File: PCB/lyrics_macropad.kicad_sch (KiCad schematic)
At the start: 8 parts, among them SW1 SW_Push, SW2 SW_Push, SW3 SW_Push, SW4 SW_Push, SW5 SW_Push, U1 XIAO-RP2040-DIP

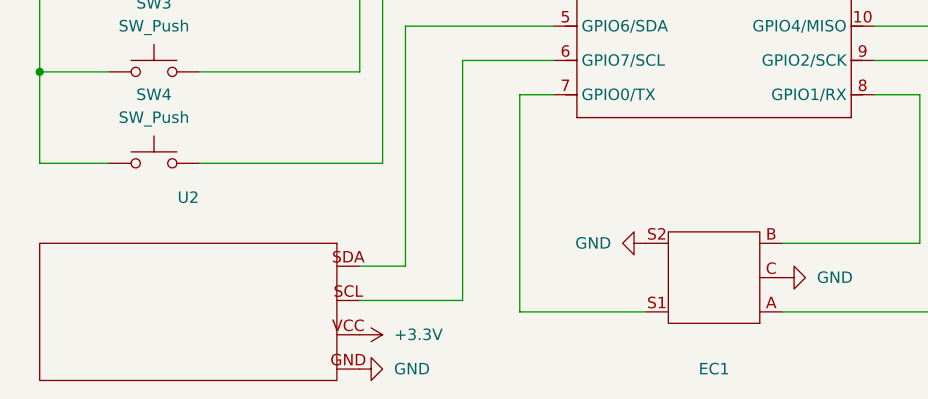
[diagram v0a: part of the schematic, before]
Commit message: Add CAD files and update PCB
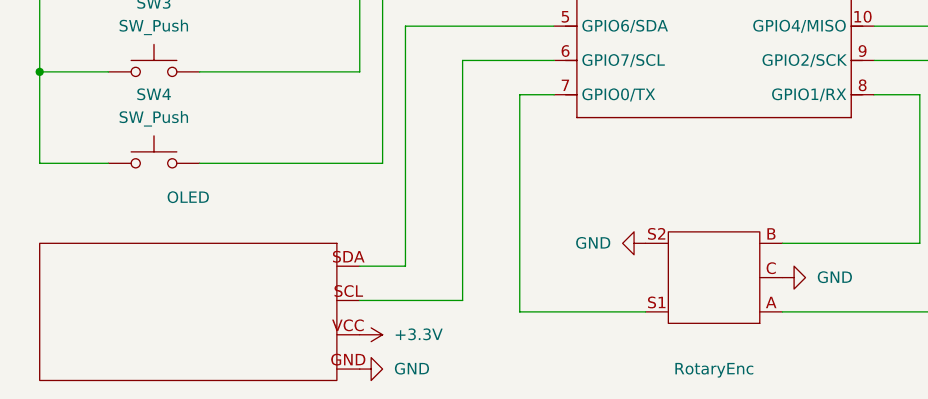
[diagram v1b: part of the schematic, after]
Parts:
- renumbered U2 to OLED, EC1 to RotaryEnc
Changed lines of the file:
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@@
 		(dnp no)
 		(fields_autoplaced yes)
-		(property "Reference" "U2"
+		(property "Reference" "OLED"
 			(at 93.98 90.17 0)
 			(effects
@@
 			(project ""
 				(path "/fcce1192-ab6a-46a7-9fac-1646581195fc"
-					(reference "U2")
+					(reference "OLED")
 					(unit 1)
 				)
@@
 		(on_board yes)
 		(dnp no)
-		(property "Reference" "EC1"
+		(property "Reference" "RotaryEnc"
 			(at 152.4 109.22 0)
 			(effects
@@
 			(project ""
 				(path "/fcce1192-ab6a-46a7-9fac-1646581195fc"
-					(reference "EC1")
-					(unit 1)
-				)
+					(reference "RotaryEnc")
+					(unit 1)
+				)
